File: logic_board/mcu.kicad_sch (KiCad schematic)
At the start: 31 parts, among them J2 SOICBite, SW1 SW_Push, SW2 SW_Push, SW3 SW_Push, SW4 SW_Push, U1 STM32H7B0RBTx, Y1 8Mhz

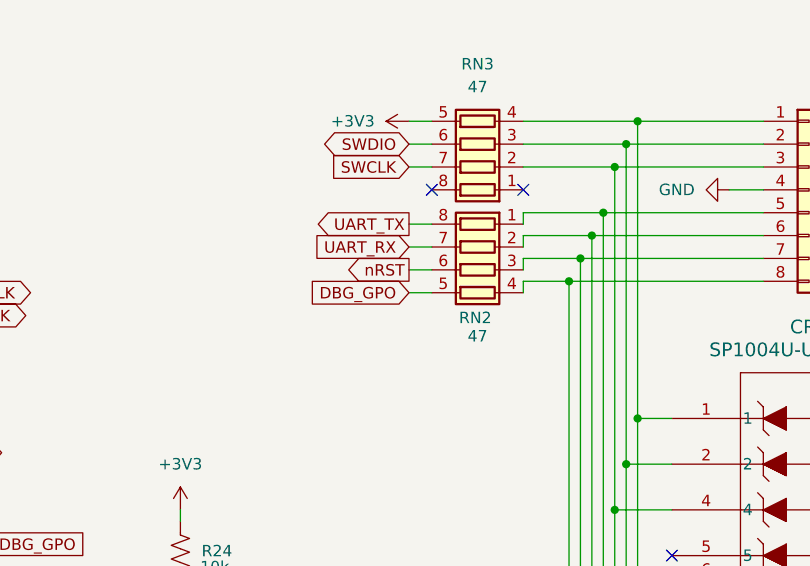
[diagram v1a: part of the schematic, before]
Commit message: Fix orientation of CR2 TVS diodes
It was turned around from the one next to it, which didn't break anything
but was bugging me.
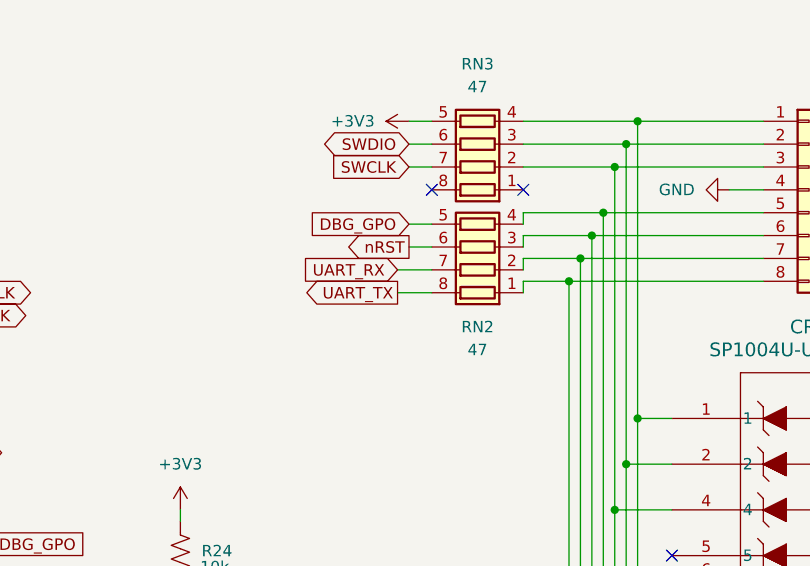
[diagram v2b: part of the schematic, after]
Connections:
- net at CR2.1, CR2.10, J2.5 (Pin_5): now also RN2.4 (R4.1); no longer RN2.1 (R1.1)
- net at CR2.2, CR2.9, J2.6 (Pin_6): now also RN2.3 (R3.1); no longer RN2.2 (R2.1)
- net at CR2.4, CR2.7, J2.7 (Pin_7): now also RN2.2 (R2.1); no longer RN2.3 (R3.1)
- net at CR2.5, CR2.6, J2.8 (Pin_8): now also RN2.1 (R1.1); no longer RN2.4 (R4.1)
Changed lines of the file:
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@@
 	(wire
 		(pts
+			(xy 210.82 39.37) (xy 213.36 39.37)
+		)
+		(stroke
+			(width 0)
+			(type default)
+		)
+	)
+	(wire
+		(pts
 			(xy 147.32 153.67) (xy 147.32 157.48)
 		)
@@
 	(wire
 		(pts
-			(xy 210.82 46.99) (xy 213.36 46.99)
-		)
-		(stroke
-			(width 0)
-			(type default)
-		)
-	)
-	(wire
-		(pts
 			(xy 124.46 168.91) (xy 135.89 168.91)
 		)
@@
 	(wire
 		(pts
-			(xy 210.82 41.91) (xy 213.36 41.91)
+			(xy 209.55 44.45) (xy 213.36 44.45)
 		)
 		(stroke
@@
 	(wire
 		(pts
-			(xy 210.82 44.45) (xy 213.36 44.45)
+			(xy 210.82 41.91) (xy 213.36 41.91)
 		)
 		(stroke
@@
 	(wire
 		(pts
-			(xy 210.82 39.37) (xy 213.36 39.37)
+			(xy 209.55 46.99) (xy 213.36 46.99)
 		)
 		(stroke
@@
 	(global_label "DBG_GPO"
 		(shape input)
-		(at 210.82 46.99 180)
+		(at 210.82 39.37 180)
 		(fields_autoplaced yes)
 		(effects
@@
 		)
 		(property "Intersheetrefs" "${INTERSHEET_REFS}"
-			(at 199.1867 46.99 0)
+			(at 199.1867 39.37 0)
 			(effects
 				(font
@@
 	(global_label "UART_RX"
 		(shape input)
-		(at 210.82 41.91 180)
+		(at 209.55 44.45 180)
 		(fields_autoplaced yes)
 		(effects
@@
 		)
 		(property "Intersheetrefs" "${INTERSHEET_REFS}"
-			(at 199.731 41.91 0)
+			(at 198.461 44.45 0)
 			(effects
 				(font
@@
 	(global_label "nRST"
 		(shape output)
-		(at 210.82 44.45 180)
+		(at 210.82 41.91 180)
 		(fields_autoplaced yes)
 		(effects
@@
 		)
 		(property "Intersheetrefs" "${INTERSHEET_REFS}"
-			(at 203.2387 44.45 0)
+			(at 203.2387 41.91 0)
 			(effects
 				(font
@@
 	(global_label "UART_TX"
 		(shape output)
-		(at 210.82 39.37 180)
+		(at 209.55 46.99 180)
 		(fields_autoplaced yes)
 		(effects
@@
 		)
 		(property "Intersheetrefs" "${INTERSHEET_REFS}"
-			(at 200.0334 39.37 0)
+			(at 198.7634 46.99 0)
 			(effects
 				(font
@@
 	(symbol
 		(lib_id "Device:R_Pack04")
-		(at 218.44 44.45 90)
-		(mirror x)
+		(at 218.44 41.91 90)
 		(unit 1)
 		(exclude_from_sim no)
@@
 		(on_board yes)
 		(dnp no)
+		(fields_autoplaced yes)
 		(property "Reference" "RN2"
-			(at 218.186 49.784 90)
+			(at 218.44 50.8 90)
 			(effects
 				(font
@@
 		)
 		(property "Value" "47"
-			(at 218.44 51.816 90)
+			(at 218.44 53.34 90)
 			(effects
 				(font
@@
 		)
 		(property "Footprint" "Resistor_SMD:R_Array_Concave_4x0603"
-			(at 218.44 51.435 90)
+			(at 218.44 34.925 90)
 			(effects
 				(font
@@
 		)
 		(property "Datasheet" "~"
-			(at 218.44 44.45 0)
+			(at 218.44 41.91 0)
 			(effects
 				(font
@@
 		)
 		(property "Description" "4 resistor network, parallel topology"
-			(at 218.44 44.45 0)
+			(at 218.44 41.91 0)
 			(effects
 				(font
@@
 		)
 		(property "LCSC Part Number" "C16081"
-			(at 218.44 44.45 90)
+			(at 218.44 41.91 90)
 			(effects
 				(font
@@
 		)
 		(instances
-			(project ""
+			(project "logic_board"
 				(path "/b7b37fe1-b409-497a-9440-d94d882f6459/bab78c00-64d8-4e72-b9b2-c8e2bf935ca1"
 					(reference "RN2")

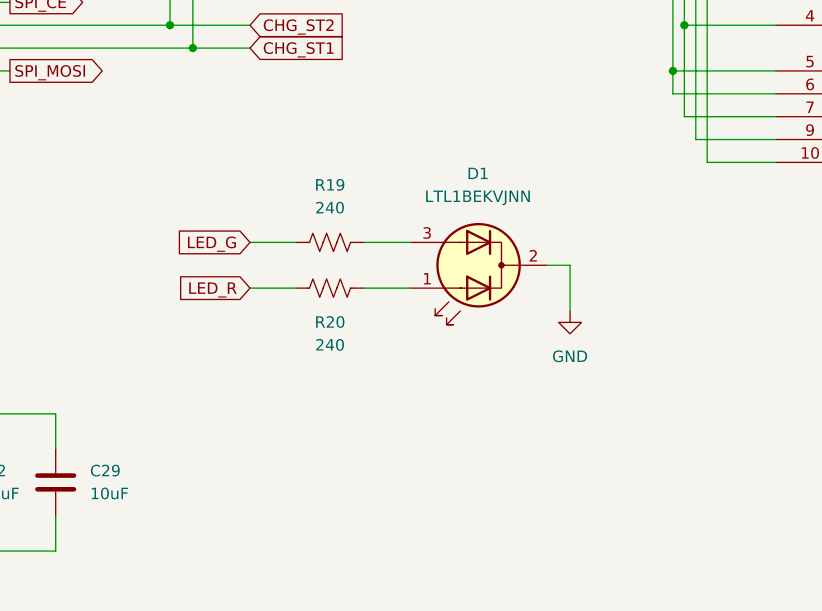
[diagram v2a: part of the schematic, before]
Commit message: Switch to buck power converter
There's a small battery life win, but some basic calculations suggested the LDO would get pretty hot.
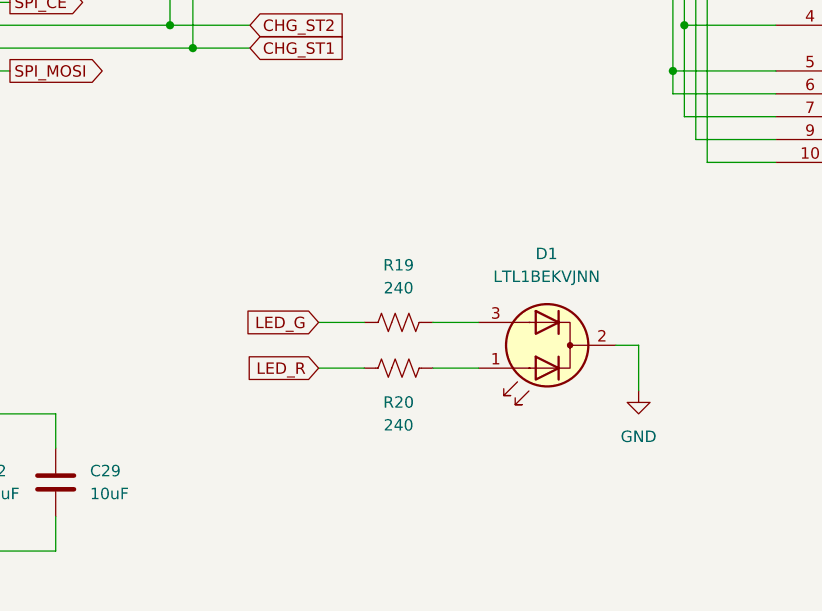
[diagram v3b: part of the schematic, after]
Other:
- moved on the sheet: D1, R19, R20
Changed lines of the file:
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@@
 	(wire
 		(pts
-			(xy 217.17 137.16) (xy 217.17 142.24)
+			(xy 224.79 146.05) (xy 224.79 151.13)
 		)
 		(stroke
@@
 	(wire
 		(pts
-			(xy 181.61 134.62) (xy 186.69 134.62)
+			(xy 189.23 143.51) (xy 194.31 143.51)
 		)
 		(stroke
@@
 	(wire
 		(pts
-			(xy 194.31 139.7) (xy 199.39 139.7)
+			(xy 201.93 148.59) (xy 207.01 148.59)
 		)
 		(stroke
@@
 	(wire
 		(pts
-			(xy 181.61 139.7) (xy 186.69 139.7)
+			(xy 189.23 148.59) (xy 194.31 148.59)
 		)
 		(stroke
@@
 	(wire
 		(pts
-			(xy 194.31 134.62) (xy 199.39 134.62)
+			(xy 201.93 143.51) (xy 207.01 143.51)
 		)
 		(stroke
@@
 	(wire
 		(pts
-			(xy 214.63 137.16) (xy 217.17 137.16)
+			(xy 222.25 146.05) (xy 224.79 146.05)
 		)
 		(stroke
@@
 	(global_label "LED_G"
 		(shape input)
-		(at 181.61 134.62 180)
+		(at 189.23 143.51 180)
 		(fields_autoplaced yes)
 		(effects
@@
 		)
 		(property "Intersheetrefs" "${INTERSHEET_REFS}"
-			(at 172.9401 134.62 0)
+			(at 180.5601 143.51 0)
 			(effects
 				(font
@@
 	(global_label "LED_R"
 		(shape input)
-		(at 181.61 139.7 180)
+		(at 189.23 148.59 180)
 		(fields_autoplaced yes)
 		(effects
@@
 		)
 		(property "Intersheetrefs" "${INTERSHEET_REFS}"
-			(at 172.9401 139.7 0)
+			(at 180.5601 148.59 0)
 			(effects
 				(font
@@
 	(symbol
 		(lib_id "Device:LED_Dual_AKA")
-		(at 207.01 137.16 180)
+		(at 214.63 146.05 180)
 		(unit 1)
 		(exclude_from_sim no)
@@
 		(fields_autoplaced yes)
 		(property "Reference" "D1"
-			(at 206.9465 127 0)
+			(at 214.5665 135.89 0)
 			(effects
 				(font
@@
 		)
 		(property "Value" "LTL1BEKVJNN"
-			(at 206.9465 129.54 0)
+			(at 214.5665 138.43 0)
 			(effects
 				(font
@@
 		)
 		(property "Footprint" "LED_THT:LED_D5.0mm-3"
-			(at 207.01 137.16 0)
+			(at 214.63 146.05 0)
 			(effects
 				(font
@@
 		)
 		(property "Datasheet" "~"
-			(at 207.01 137.16 0)
+			(at 214.63 146.05 0)
 			(effects
 				(font
@@
 		)
 		(property "Description" "Dual LED, common cathode on pin 2"
-			(at 207.01 137.16 0)
+			(at 214.63 146.05 0)
 			(effects
 				(font
@@
 	(symbol
 		(lib_id "Device:R_US")
-		(at 190.5 134.62 90)
+		(at 198.12 143.51 90)
 		(unit 1)
 		(exclude_from_sim no)
@@
 		(fields_autoplaced yes)
 		(property "Reference" "R19"
-			(at 190.5 128.27 90)
+			(at 198.12 137.16 90)
 			(effects
 				(font
@@
 		)
 		(property "Value" "240"
-			(at 190.5 130.81 90)
+			(at 198.12 139.7 90)
 			(effects
 				(font
@@
 		)
 		(property "Footprint" "Resistor_SMD:R_0603_1608Metric"
-			(at 190.754 133.604 90)
+			(at 198.374 142.494 90)
 			(effects
 				(font
@@
 		)
 		(property "Datasheet" "~"
-			(at 190.5 134.62 0)
+			(at 198.12 143.51 0)
 			(effects
 				(font
@@
 		)
 		(property "Description" "Resistor, US symbol"
-			(at 190.5 134.62 0)
+			(at 198.12 143.51 0)
 			(effects
 				(font
@@
 		)
 		(property "LCSC Part Number" "C23350"
-			(at 190.5 134.62 90)
+			(at 198.12 143.51 90)
 			(effects
 				(font
@@
 	(symbol
 		(lib_id "power:GND")
-		(at 217.17 142.24 0)
+		(at 224.79 151.13 0)
 		(unit 1)
 		(exclude_from_sim no)
@@
 		(fields_autoplaced yes)
 		(property "Reference" "#PWR052"
-			(at 217.17 148.59 0)
+			(at 224.79 157.48 0)
 			(effects
 				(font
@@
 		)
 		(property "Value" "GND"
-			(at 217.17 147.32 0)
+			(at 224.79 156.21 0)
 			(effects
 				(font
@@
 		)
 		(property "Footprint" ""
-			(at 217.17 142.24 0)
+			(at 224.79 151.13 0)
 			(effects
 				(font
@@
 		)
 		(property "Datasheet" ""
-			(at 217.17 142.24 0)
+			(at 224.79 151.13 0)
 			(effects
 				(font
@@
 		)
 		(property "Description" "Power symbol creates a global label with name \"GND\" , ground"
-			(at 217.17 142.24 0)
+			(at 224.79 151.13 0)
 			(effects
 				(font
@@
 	(symbol
 		(lib_id "Device:R_US")
-		(at 190.5 139.7 90)
+		(at 198.12 148.59 90)
 		(unit 1)
 		(exclude_from_sim no)
@@
 		(fields_autoplaced yes)
 		(property "Reference" "R20"
-			(at 190.5 143.51 90)
+			(at 198.12 152.4 90)
 			(effects
 				(font
@@
 		)
 		(property "Value" "240"
-			(at 190.5 146.05 90)
+			(at 198.12 154.94 90)
 			(effects
 				(font
@@
 		)
 		(property "Footprint" "Resistor_SMD:R_0603_1608Metric"
-			(at 190.754 138.684 90)
+			(at 198.374 147.574 90)
 			(effects
 				(font
@@
 		)
 		(property "Datasheet" "~"
-			(at 190.5 139.7 0)
+			(at 198.12 148.59 0)
 			(effects
 				(font
@@
 		)
 		(property "Description" "Resistor, US symbol"
-			(at 190.5 139.7 0)
+			(at 198.12 148.59 0)
 			(effects
 				(font
@@
 		)
 		(property "LCSC Part Number" "C23350"
-			(at 190.5 139.7 90)
+			(at 198.12 148.59 90)
 			(effects
 				(font

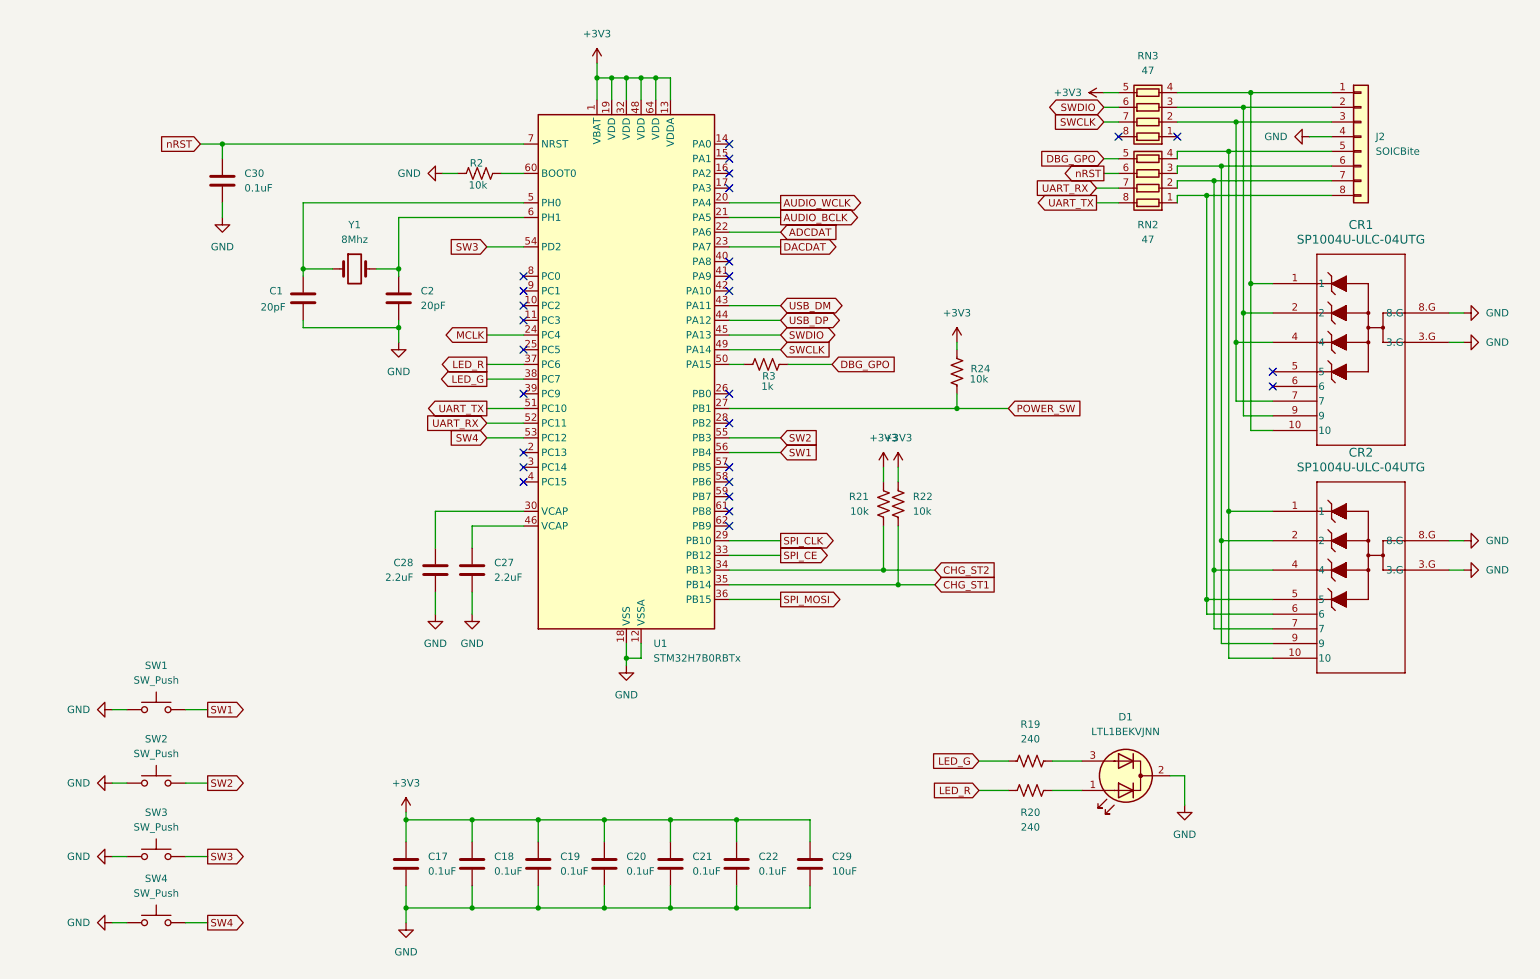
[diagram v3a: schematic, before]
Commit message: Add test points, schematic annotations
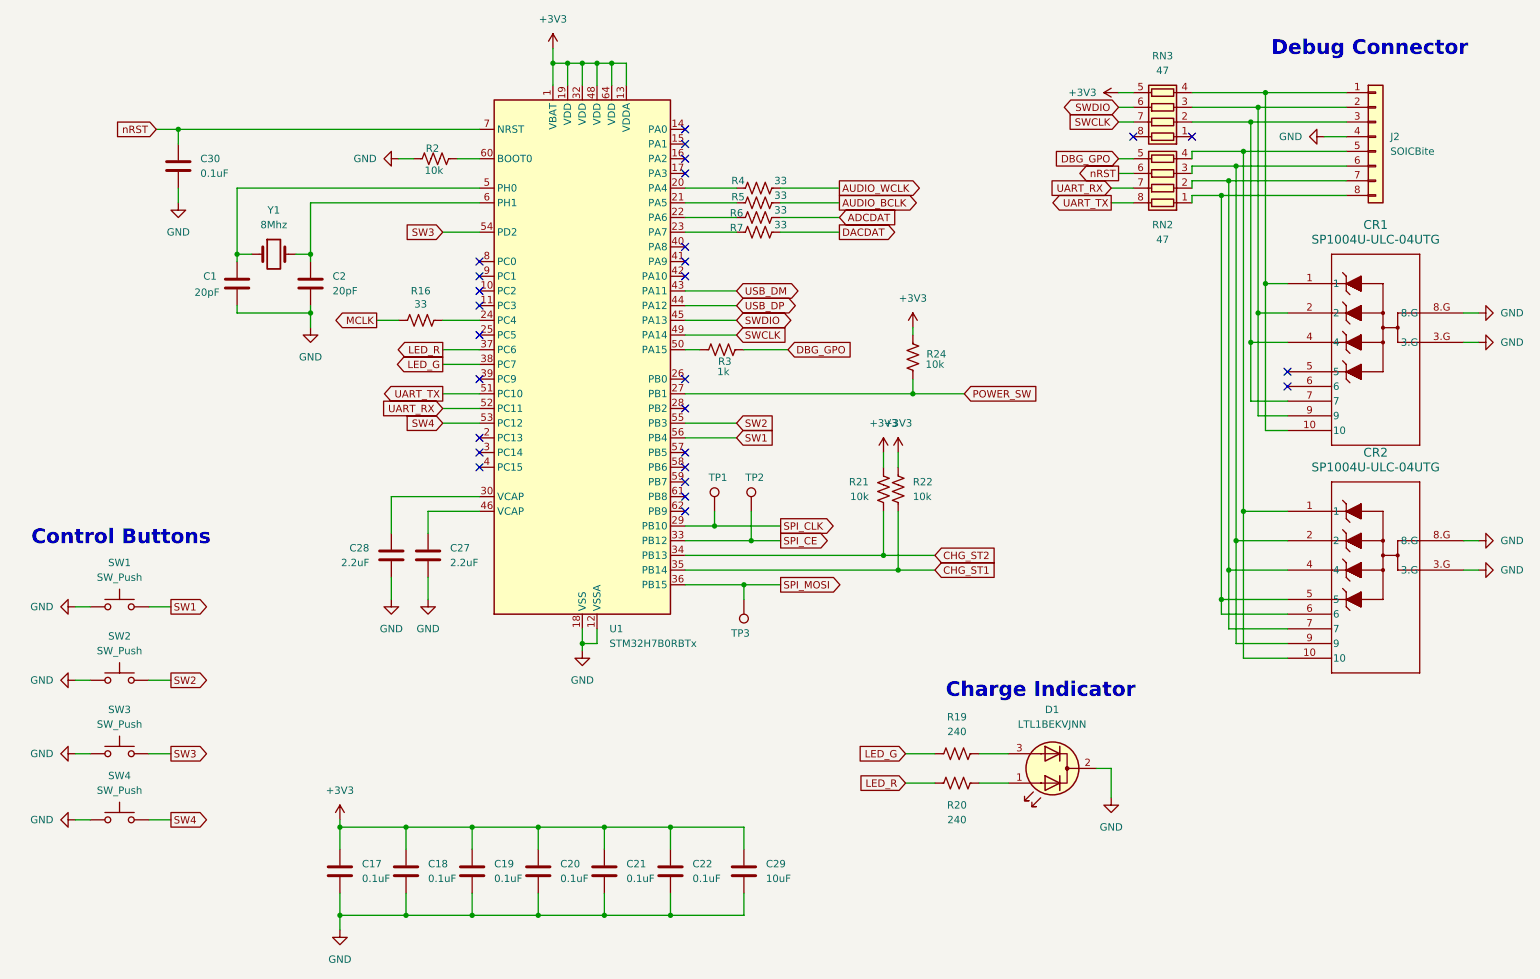
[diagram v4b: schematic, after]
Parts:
- added R16, R4, R5, R6, R7: 33, Resistor_SMD:R_0603_1608Metric, symbol Device:R_US
- added TP1, TP2, TP3: TestPoint, TestPoint:TestPoint_Pad_D1.0mm, symbol Connector:TestPoint
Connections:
- net ADCDAT: now also R6.2; no longer U1.22 (PA6)
- net AUDIO_BCLK: now also R5.2; no longer U1.21 (PA5)
- net AUDIO_WCLK: now also R4.2; no longer U1.20 (PA4)
- net DACDAT: now also R7.2; no longer U1.23 (PA7)
- net MCLK: now also R16.1; no longer U1.24 (PC4)
- net SPI_CE: now also TP2.1
- net SPI_CLK: now also TP1.1
- net SPI_MOSI: now also TP3.1
- new net: R4.1, U1.20 (PA4)
- new net: R5.1, U1.21 (PA5)
- new net: R6.1, U1.22 (PA6)
- new net: R7.1, U1.23 (PA7)
- new net: R16.2, U1.24 (PC4)
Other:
- note added: "Charge Indicator"
- note added: "Control Buttons"
- note added: "Debug Connector"
- moved on the sheet: C1, C17, C18, C19, C2, C20, C21, C22, C27, C28, C29, C30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

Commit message: Change to resistor network for I2S termination resistors to save space Also remove 1k resistor from debug GPIO, as it is unnecessary.
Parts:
- removed R3: 1k, Resistor_SMD:R_0603_1608Metric, symbol Device:R_US
- removed R4, R5, R6, R7: 33, Resistor_SMD:R_0603_1608Metric, symbol Device:R_US
- added RN1: 47, Resistor_SMD:R_Array_Concave_4x0603, symbol Device:R_Pack04
- R16: value 33 -> 47; LCSC Part Number C23140 -> (none)
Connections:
- net ADCDAT: now also RN1.5 (R4.2)
- net AUDIO_BCLK: now also RN1.8 (R1.2)
- net AUDIO_WCLK: now also RN1.6 (R3.2)
- net DACDAT: now also RN1.7 (R2.2)
- net DBG_GPO: now also U1.50 (PA15)
- net at U1.20 (PA4): now also RN1.1 (R1.1)
- net at U1.21 (PA5): now also RN1.2 (R2.1)
- net at U1.22 (PA6): now also RN1.3 (R3.1)
- net at U1.23 (PA7): now also RN1.4 (R4.1)

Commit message: Minor cosmetic tweaks, fix silkscreen references
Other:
- title: (none) -> Microcontroller and User Interface
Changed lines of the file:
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@@
 	(generator_version "9.0")
 	(paper "A4")
+	(title_block
+		(title "Microcontroller and User Interface")
+		(date "2026-01-02")
+		(rev "2.0")
+	)
 	(text "Control Buttons"
 		(exclude_from_sim no)
